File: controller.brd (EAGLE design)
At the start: 42.8 x 36.8 mm, 23 parts, among them U1 10118194-MICRO-USB, U2 LM3671MF-3.3/NOPBMF05A-M, U3 SN74LVC1T45DBVRDBV6-M, U4 SN74LVC1T45DBVRDBV6-M

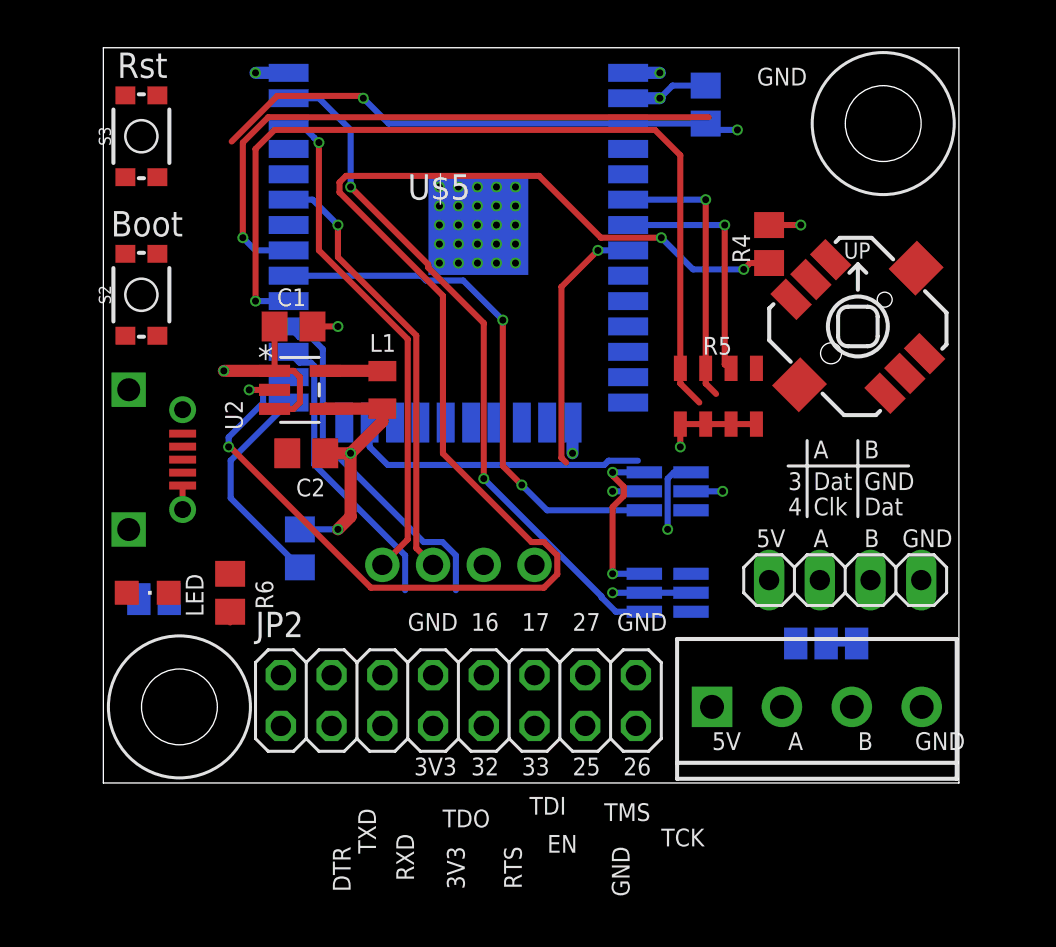
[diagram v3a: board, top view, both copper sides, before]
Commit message: Finished placing parts
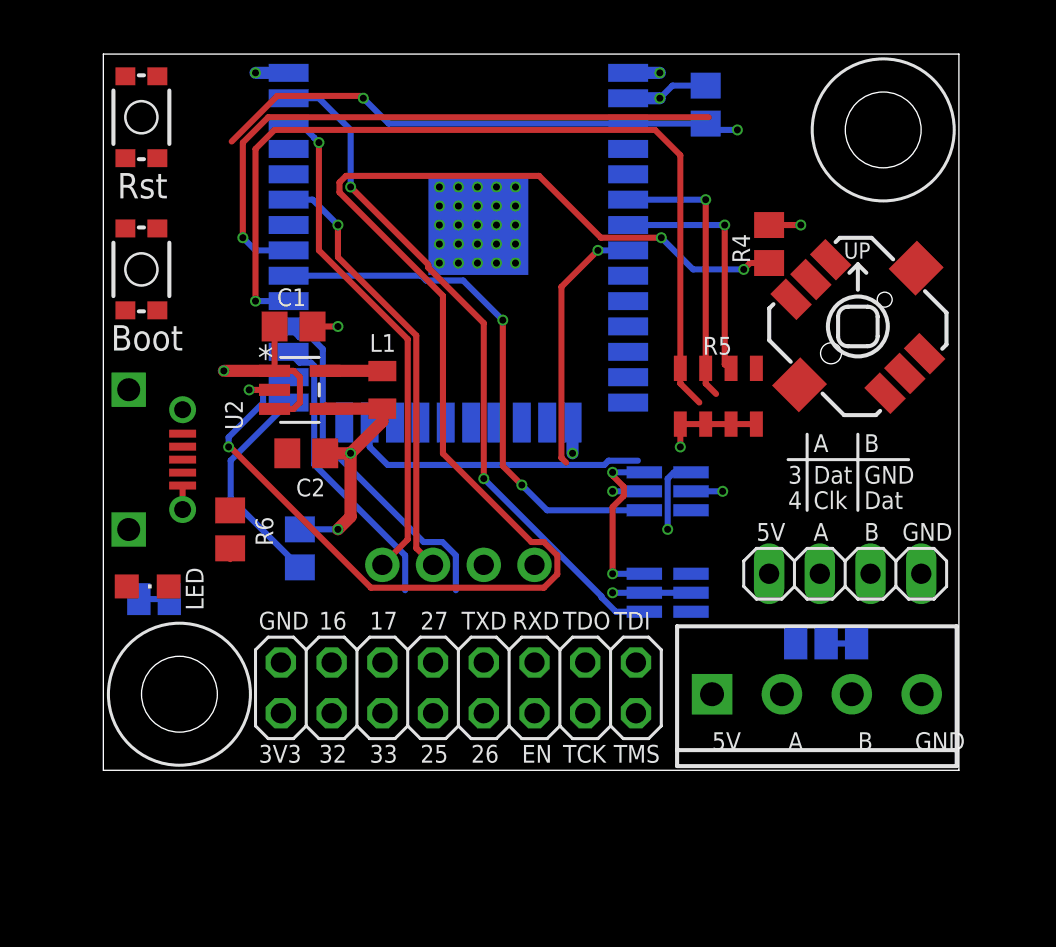
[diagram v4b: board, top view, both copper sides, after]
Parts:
- moved R6 3.18 mm to (87.6, 58.4)
- moved S2 1.27 mm to (83.2, 71.4)
- moved S3 0.95 mm to (83.2, 79.1)
- moved JP2 0.64 mm to (99.1, 50.5)
- moved J1 0.63 mm to (111.8, 50.2)
- moved LED1 0.32 mm to (83.5, 55.6)
- moved JP1 0.32 mm to (118.4, 56.2)
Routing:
- net VCC: track 32.5 -> 34.0 mm
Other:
- board size 42.8 x 36.8 mm -> 42.8 x 35.9 mm
- board text added: "Power LED"
- board text removed: "DTR"
- board text removed: "RTS"

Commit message: Finished v1.2
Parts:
- moved R7 15.1 mm to (86.8, 71.9)
- moved R4 1.12 mm to (114.5, 73.8)
- moved SJ2 0.32 mm to (83.5, 54.9)
- turned JP2 to 180 degrees
- turned S3 to 270 degrees
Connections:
- removed net N$2: JP2.2
- removed net N$3: C1.1, U1.1, U2.1, U2.3
- net +5V: now also C1.1, U1.1, U2.1, U2.3
- net GND: now also JP2.2
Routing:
- net TXD: track 0.00 -> 48.9 mm
- net EN: track 27.0 -> 73.1 mm
- net RXD: track 0.00 -> 42.9 mm
- net GPIO26: track 0.00 -> 38.6 mm, vias 0 -> 1
- net GPIO25: track 0.00 -> 36.1 mm, vias 0 -> 1
- net TDI: track 0.00 -> 32.5 mm, vias 0 -> 1
- net GPIO27: track 0.00 -> 32.3 mm, vias 0 -> 1
- net TMS: track 0.00 -> 30.8 mm, vias 0 -> 1
- net CENTER: track 73.7 -> 44.3 mm, vias 3 -> 1
- net GPIO33: track 0.00 -> 27.3 mm, vias 0 -> 1
- net GND: track 17.1 -> 40.2 mm, vias 33 -> 36
- net VCC: track 34.0 -> 57.2 mm, vias 7 -> 11
- net TCK: track 0.00 -> 19.7 mm, vias 0 -> 1
- net N$7: track 1.52 -> 19.5 mm
- net DOWN: track 32.1 -> 49.7 mm
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
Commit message: Version 1.3
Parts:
- added SJ3: (no value), jumper:SJ
- moved SJ1 0.32 mm to (117.8, 52.7)
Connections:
- net +5V: now also SJ3.1, SJ3.2
- net EN: no longer JP2.11
- net GND: now also JP2.11
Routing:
- net EN: track 73.1 -> 35.1 mm
- net +5V: track 18.1 -> 32.3 mm, vias 3 -> 4
- net N$7: track 19.5 -> 27.2 mm
- net GND: track 40.2 -> 35.1 mm, vias 36 -> 37
- net N$9: track 15.5 -> 17.0 mm
- added copper zone on layer 15, net N$2
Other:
- board text added: "5V LED Power"
- board text added: "RVL Controller v1.3 Copyright Bryan Hughes October 2019"
- board text removed: "EN"
- board text removed: "RVL Controller v1.2 Copyright Bryan Hughes October 2019"

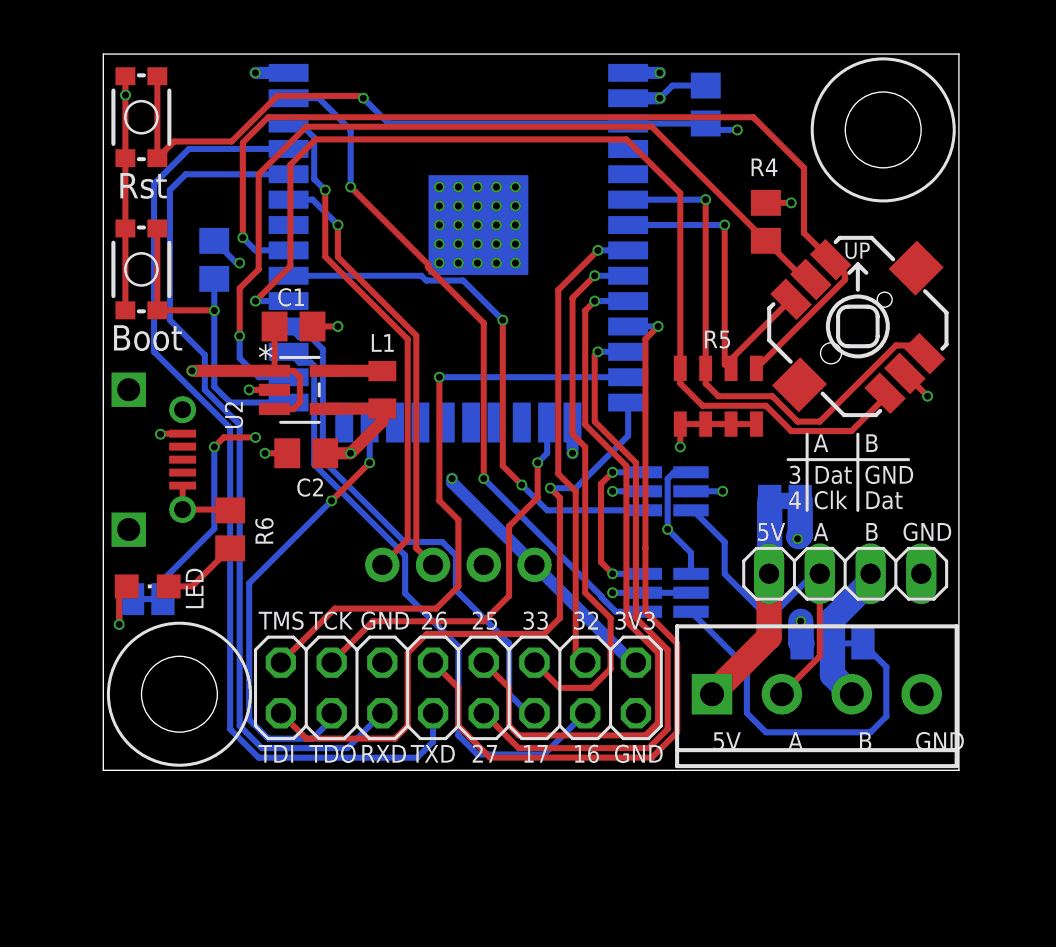
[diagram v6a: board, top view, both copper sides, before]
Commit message: Fixed pin labelling
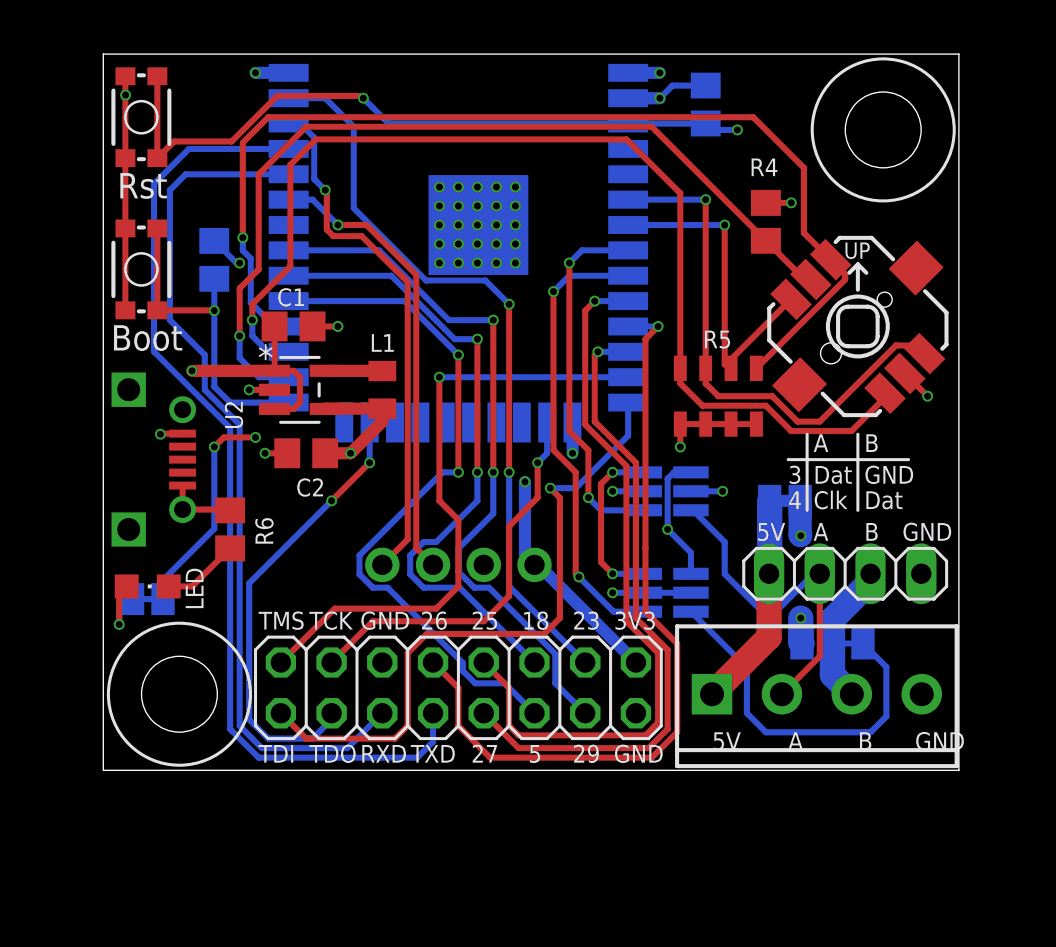
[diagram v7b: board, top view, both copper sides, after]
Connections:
- removed net GPIO16: JP2.4, U$2.27
- removed net GPIO17: JP2.6, U$2.28
- removed net GPIO32: JP2.3, U$2.8
- removed net GPIO33: JP2.5, U$2.9
- new net GPIO18: JP2.5, U$2.30
- new net GPIO19: JP2.4, U$2.31
- new net GPIO23: JP2.3, U$2.37
- new net GPIO5: JP2.6, U$2.29
- net DOWN: now also U$2.28; no longer U$2.31
- net LED_CLOCK: now also U$2.8; no longer U$2.30
- net LED_DATA: now also U$2.9; no longer U$2.37
- net UP: now also U$2.27; no longer U$2.29
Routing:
- net GPIO23: track 0.00 -> 37.2 mm, vias 0 -> 2
- net GPIO19: track 0.00 -> 35.2 mm, vias 0 -> 2
- net GPIO5: track 0.00 -> 35.0 mm, vias 0 -> 2
- net GPIO18: track 0.00 -> 32.4 mm, vias 0 -> 2
- net GPIO16: track 30.7 -> 0.00 mm
- net GPIO33: track 27.3 -> 0.00 mm, vias 1 -> 0
- net GPIO17: track 26.1 -> 0.00 mm
- net GPIO32: track 23.5 -> 0.00 mm, vias 1 -> 0
- net LED_DATA: track 34.8 -> 22.9 mm
- net LED_CLOCK: track 27.0 -> 18.4 mm
- net DOWN: track 49.7 -> 53.0 mm
- net UP: track 52.1 -> 54.4 mm
- net VCC: track 57.2 -> 55.5 mm
- net SCL: track 22.0 -> 22.8 mm
- net SDA: track 25.4 -> 26.3 mm
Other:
- board text added: "18"
- board text added: "23"
- board text added: "29"
- board text added: "5"
- board text added: "RVL Controller v1.4 Copyright Bryan Hughes March 2020"
- board text removed: "16"
- board text removed: "17"
- board text removed: "32"
- board text removed: "33"
- board text removed: "RVL Controller v1.3 Copyright Bryan Hughes October 2019"
